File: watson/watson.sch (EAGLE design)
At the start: 37 parts, among them X1 2540-FLAT

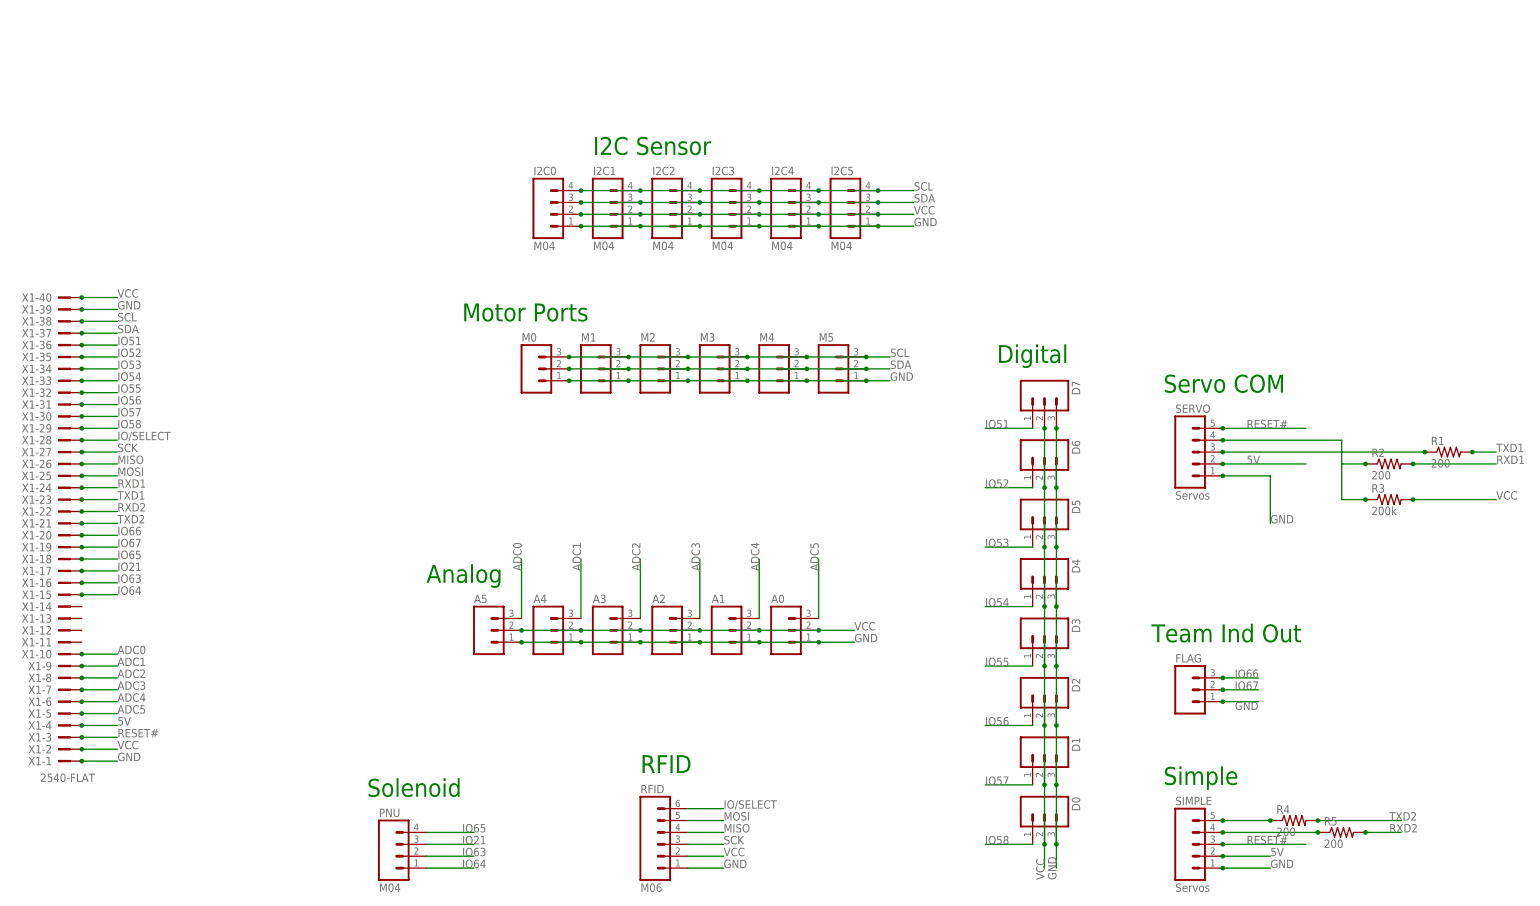
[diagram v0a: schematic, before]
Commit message: Fix all schematics to have a frame and be in quadrant I
Change-Id: I9709ffe2e940512e8f74172f888a837b658cad74
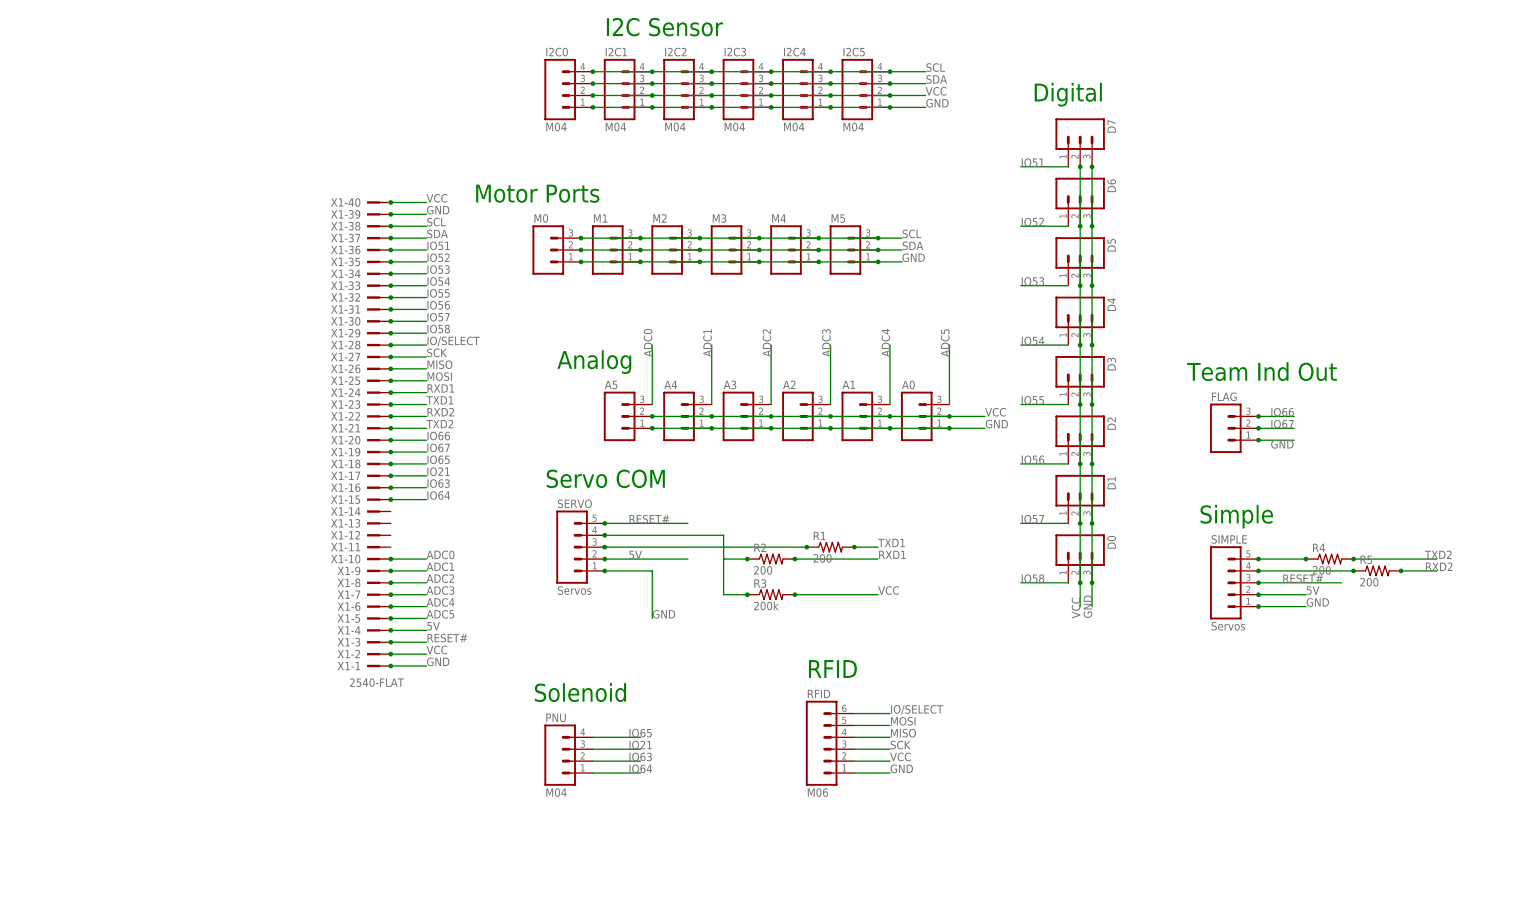
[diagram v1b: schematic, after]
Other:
- moved on the sheet: A0, A1, A2, A3, A4, A5, D0, D1, D2, D3, D4, D5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

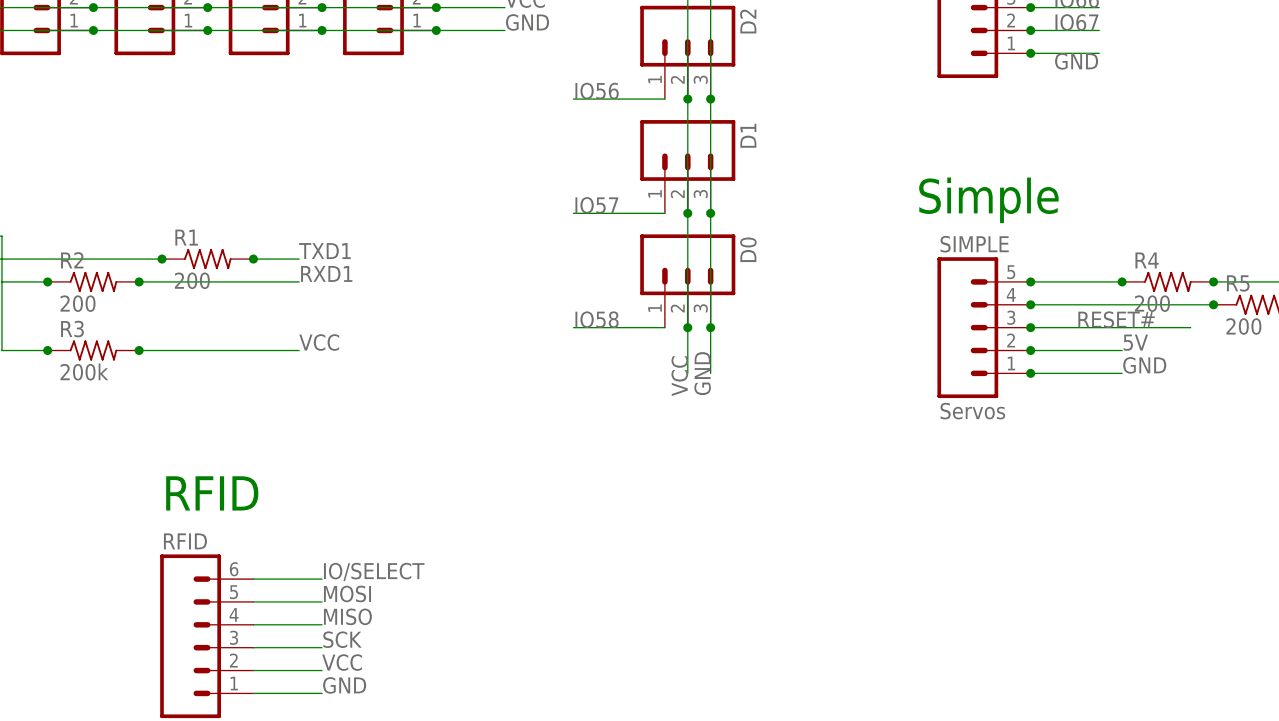
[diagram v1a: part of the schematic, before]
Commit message: Added author names and relabeled some connectors.
Change-Id: Ieedfea911c64140b2cf1aaf189780d0d3449f093
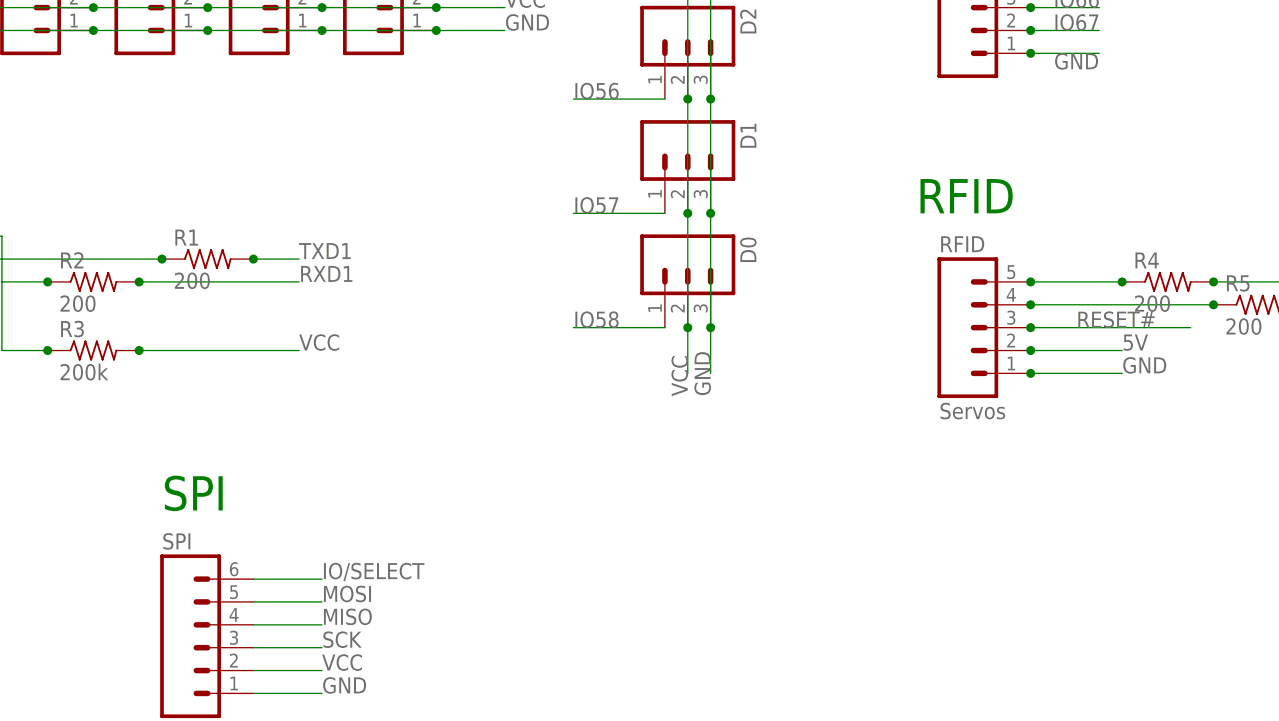
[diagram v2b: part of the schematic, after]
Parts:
- removed SIMPLE: Servos, MTA-connectors:M05
- added SPI: M06, MTA-connectors:M06
- RFID: value M06 -> Servos; device MTA-connectors:M06 -> MTA-connectors:M05
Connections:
- net 5V: now also RFID.2; no longer SIMPLE.2
- net GND: now also SPI.1; no longer SIMPLE.1
- net IO/SELECT: now also SPI.6; no longer RFID.6
- net MISO: now also SPI.4; no longer RFID.4
- net MOSI: now also SPI.5; no longer RFID.5
- net N$5: now also RFID.5; no longer SIMPLE.5
- net N$6: now also RFID.4; no longer SIMPLE.4
- net RESET#: now also RFID.3; no longer SIMPLE.3
- net SCK: now also SPI.3; no longer RFID.3
- net VCC: now also SPI.2; no longer RFID.2
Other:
- note added: "SPI"
- note removed: "Simple"
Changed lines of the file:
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@@
 <part name="I2C1" library="MTA-connectors" deviceset="M04" device=""/>
 <part name="I2C0" library="MTA-connectors" deviceset="M04" device=""/>
-<part name="RFID" library="MTA-connectors" deviceset="M06" device=""/>
+<part name="SPI" library="MTA-connectors" deviceset="M06" device=""/>
 <part name="R1" library="resistor" deviceset="R-US_" device="R0603" value="200"/>
 <part name="R2" library="resistor" deviceset="R-US_" device="R0603" value="200"/>
@@
 <attribute name="OC_FARNELL" value="unknown"/>
 </part>
-<part name="SIMPLE" library="MTA-connectors" deviceset="M05" device="" value="Servos"/>
+<part name="RFID" library="MTA-connectors" deviceset="M05" device="" value="Servos"/>
 <part name="PNU" library="MTA-connectors" deviceset="M04" device=""/>
 <part name="R5" library="resistor" deviceset="R-US_" device="R0603" value="200"/>
 <part name="R4" library="resistor" deviceset="R-US_" device="R0603" value="200"/>
 <part name="FRAME1" library="pie" deviceset="FRAME-LETTER" device="">
+<attribute name="AUTHOR" value="Michael C., Sumita G., Sahar M."/>
 <attribute name="REVISION" value="A"/>
 </part>
@@
 <text x="53.34" y="78.74" size="3.81" layer="91">Servo COM</text>
 <text x="66.04" y="175.26" size="3.81" layer="91">I2C Sensor</text>
-<text x="109.22" y="38.1" size="3.81" layer="91">RFID</text>
-<text x="193.04" y="71.12" size="3.81" layer="91">Simple</text>
+<text x="109.22" y="38.1" size="3.81" layer="91">SPI</text>
+<text x="193.04" y="71.12" size="3.81" layer="91">RFID</text>
 <text x="50.8" y="33.02" size="3.81" layer="91">Solenoid</text>
 </plain>
@@
 <instance part="I2C1" gate="G$1" x="71.12" y="165.1"/>
 <instance part="I2C0" gate="G$1" x="58.42" y="165.1"/>
-<instance part="RFID" gate="G$1" x="114.3" y="25.4"/>
+<instance part="SPI" gate="G$1" x="114.3" y="25.4"/>
 <instance part="R1" gate="G$1" x="114.3" y="66.04"/>
 <instance part="R2" gate="G$1" x="101.6" y="63.5"/>
@@
 <instance part="X1" gate="-39" x="15.24" y="137.16" rot="MR180"/>
 <instance part="X1" gate="-40" x="15.24" y="139.7" rot="MR180"/>
-<instance part="SIMPLE" gate="G$1" x="200.66" y="60.96"/>
+<instance part="RFID" gate="G$1" x="200.66" y="60.96"/>
 <instance part="PNU" gate="G$1" x="58.42" y="22.86"/>
 <instance part="R5" gate="G$1" x="231.14" y="60.96"/>
@@
 <instance part="FRAME1" gate="G$2" x="147.32" y="0">
 <attribute name="REVISION" x="147.32" y="0" size="1.778" layer="96" display="off"/>
+<attribute name="AUTHOR" x="147.32" y="0" size="1.778" layer="96" display="off"/>
 </instance>
 </instances>
@@
 </segment>
 <segment>
-<pinref part="RFID" gate="G$1" pin="1"/>
+<pinref part="SPI" gate="G$1" pin="1"/>
 <wire x1="119.38" y1="17.78" x2="127" y2="17.78" width="0.1524" layer="91"/>
 <label x="127" y="17.78" size="1.778" layer="95"/>
@@
 </segment>
 <segment>
-<pinref part="SIMPLE" gate="G$1" pin="1"/>
+<pinref part="RFID" gate="G$1" pin="1"/>
 <wire x1="205.74" y1="53.34" x2="215.9" y2="53.34" width="0.1524" layer="91"/>
 <junction x="205.74" y="53.34"/>
@@
 </segment>
 <segment>
-<pinref part="RFID" gate="G$1" pin="2"/>
+<pinref part="SPI" gate="G$1" pin="2"/>
 <wire x1="119.38" y1="20.32" x2="127" y2="20.32" width="0.1524" layer="91"/>
 <label x="127" y="20.32" size="1.778" layer="95"/>
@@
 <net name="MOSI" class="0">
 <segment>
-<pinref part="RFID" gate="G$1" pin="5"/>
+<pinref part="SPI" gate="G$1" pin="5"/>
 <wire x1="119.38" y1="27.94" x2="127" y2="27.94" width="0.1524" layer="91"/>
 <label x="127" y="27.94" size="1.778" layer="95"/>
@@
 <net name="MISO" class="0">
 <segment>
-<pinref part="RFID" gate="G$1" pin="4"/>
+<pinref part="SPI" gate="G$1" pin="4"/>
 <wire x1="119.38" y1="25.4" x2="127" y2="25.4" width="0.1524" layer="91"/>
 <label x="127" y="25.4" size="1.778" layer="95"/>
@@
 <net name="SCK" class="0">
 <segment>
-<pinref part="RFID" gate="G$1" pin="3"/>
+<pinref part="SPI" gate="G$1" pin="3"/>
 <wire x1="119.38" y1="22.86" x2="127" y2="22.86" width="0.1524" layer="91"/>
 <label x="127" y="22.86" size="1.778" layer="95"/>
@@
 </segment>
 <segment>
-<pinref part="SIMPLE" gate="G$1" pin="3"/>
+<pinref part="RFID" gate="G$1" pin="3"/>
 <wire x1="205.74" y1="58.42" x2="223.52" y2="58.42" width="0.1524" layer="91"/>
 <junction x="205.74" y="58.42"/>
@@
 </segment>
 <segment>
-<pinref part="SIMPLE" gate="G$1" pin="2"/>
+<pinref part="RFID" gate="G$1" pin="2"/>
 <wire x1="205.74" y1="55.88" x2="215.9" y2="55.88" width="0.1524" layer="91"/>
 <junction x="205.74" y="55.88"/>
@@
 <net name="IO/SELECT" class="0">
 <segment>
-<pinref part="RFID" gate="G$1" pin="6"/>
+<pinref part="SPI" gate="G$1" pin="6"/>
 <wire x1="119.38" y1="30.48" x2="127" y2="30.48" width="0.1524" layer="91"/>
 <label x="127" y="30.48" size="1.778" layer="95"/>
@@
 <net name="N$5" class="0">
 <segment>
-<pinref part="SIMPLE" gate="G$1" pin="5"/>
+<pinref part="RFID" gate="G$1" pin="5"/>
 <wire x1="205.74" y1="63.5" x2="215.9" y2="63.5" width="0.1524" layer="91"/>
 <pinref part="R4" gate="G$1" pin="1"/>
@@
 <net name="N$6" class="0">
 <segment>
-<pinref part="SIMPLE" gate="G$1" pin="4"/>
+<pinref part="RFID" gate="G$1" pin="4"/>
 <pinref part="R5" gate="G$1" pin="1"/>
 <wire x1="205.74" y1="60.96" x2="226.06" y2="60.96" width="0.1524" layer="91"/>
